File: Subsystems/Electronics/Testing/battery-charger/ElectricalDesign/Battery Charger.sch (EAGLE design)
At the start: 98 parts, among them J1 USB4515-GF-A_REVA, Q1 CSD16406Q3, Q2 CSD16406Q3, Q3 DMN2008LFU, Q4 DMN2008LFU, Q5 DMN2008LFU, Q6 BC817, Q7 BC817, U1 BQ24650, U2 BQ29700, U3 BQ29700, U4 BQ29700, U5 CP2102N-A02-GQFN28, U7 ESP32-S2-MINI-1

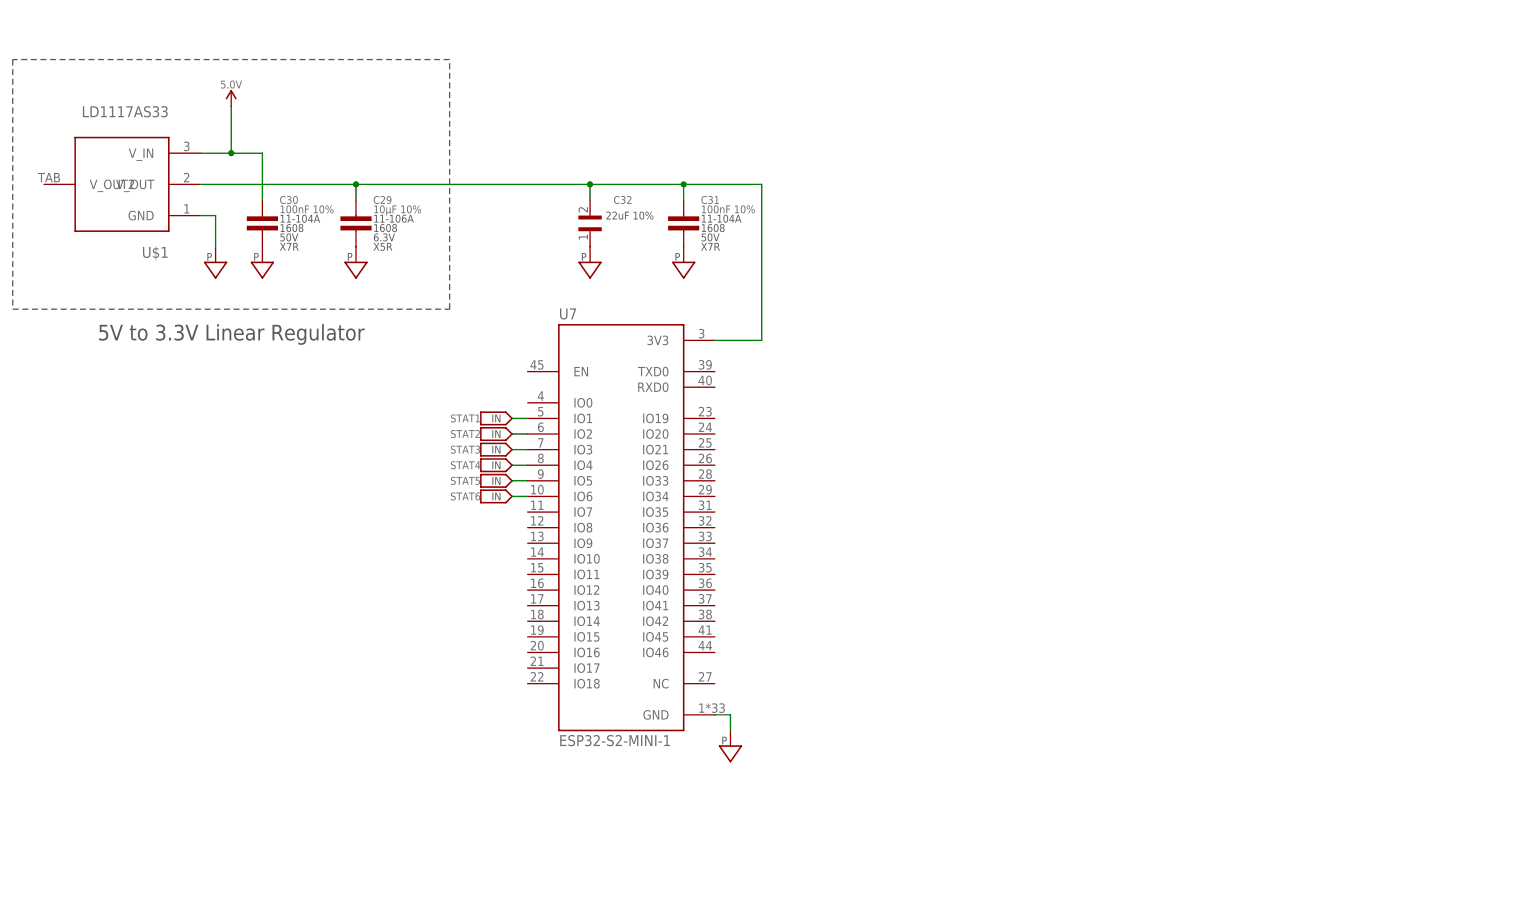
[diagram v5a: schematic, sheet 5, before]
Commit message: Finished Battery Charger V1
Will add programmable RGB LEDS at some point, and may update at a later date with an LED display, but otherwise this can be considered the base design for the over-engineered battery charger
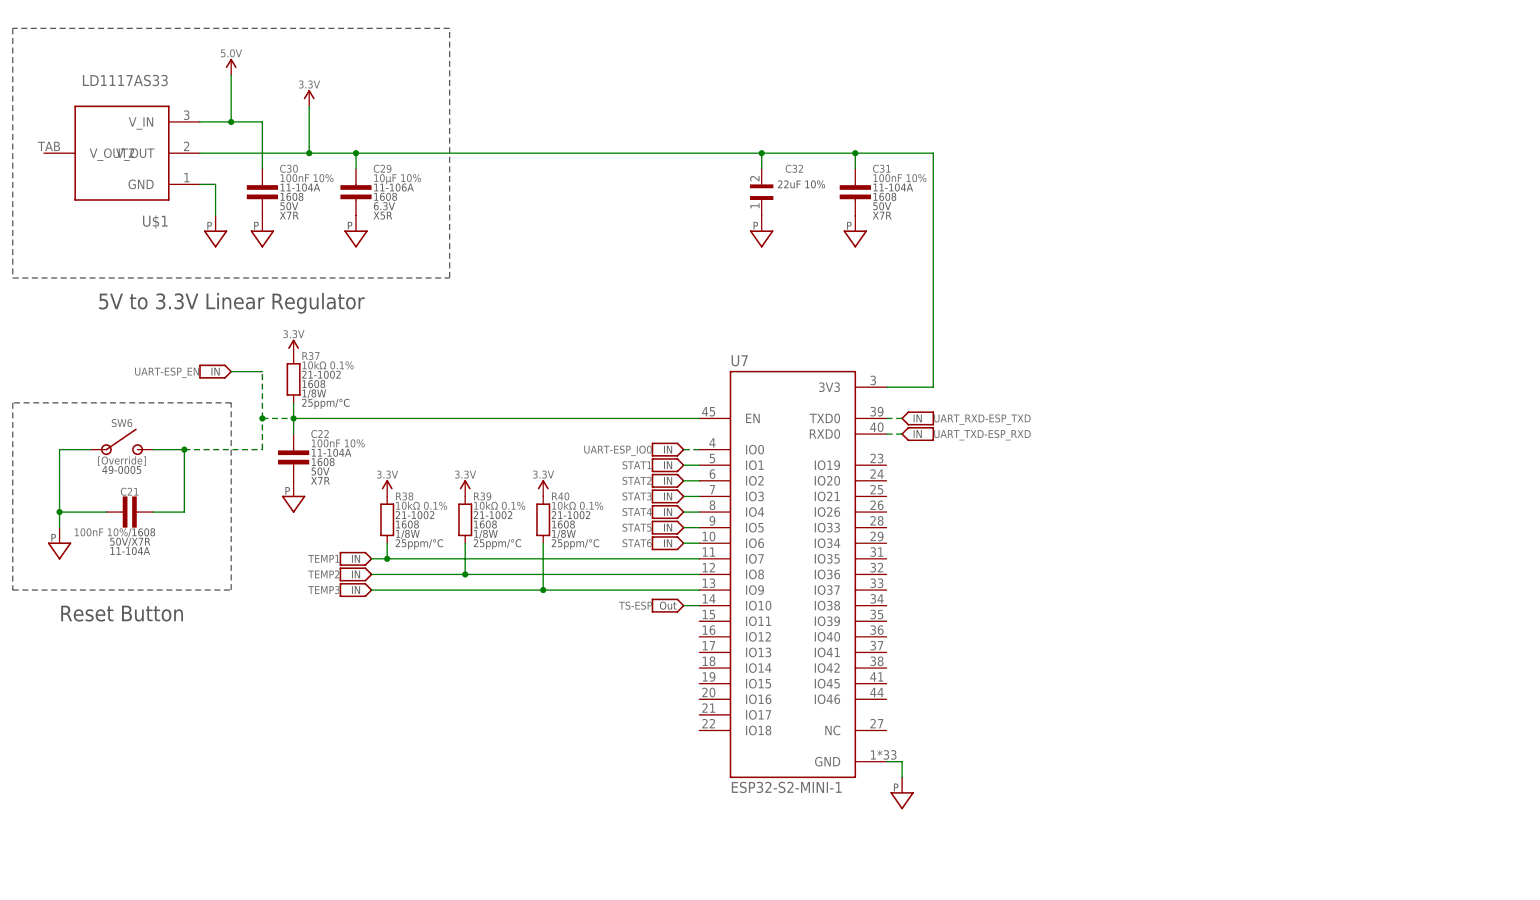
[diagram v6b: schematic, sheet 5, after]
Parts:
- removed J2: (no value), CougsInSpace-Connectors:USB-B-FEMALE
- added C21: 100nF 10%, CougsInSpace-Capacitors:CAP-H-100NF-1608
- added C22: 100nF 10%, CougsInSpace-Capacitors:CAP-V-100NF-1608
- added J3: 10103592-0001LF, 10103592-0001LF:10103592-0001LF
- added R37, R38, R39, R40: 10kΩ 0.1%, CougsInSpace-Resistors:RES-V-10K-1608
- added RT1, RT2, RT3: 10kΩ 5%, CougsInSpace-Resistors:THERMISTOR-V-10K-1608
- added SW6: [Override], CougsInSpace-Switches:SWITCH-SPST-NO-B3F-1050-THT-6060
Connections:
- removed net N$44: C29.1, C31.1, C32.2, U$1.V_OUT, U7.3V3
- new net 3.3V: C29.1, C31.1, C32.2, R37.2, R38.2, R39.2, R40.2, U$1.V_OUT, U7.3V3
- new net TEMP1: R38.1, RT1.2, U7.IO7
- new net TEMP2: R39.1, RT2.2, U7.IO8
- new net TEMP3: R40.1, RT3.2, U7.IO9
- new net TS-ESP: U1.TS, U7.IO10
- net N$25: now also J3.D+; no longer J2.DATA_P
- net N$31: now also J3.D-; no longer J2.DATA_N
- net N$42: now also J3.VDD; no longer J2.VCC
- net PGND: now also C21.1, C22.2, J3.GND, J3.SHIELD, RT1.1, RT2.1, RT3.1, SW6.COM; no longer J2.GND, J2.SHIELD
- net UART-ESP_EN: now also C21.2, C22.1, R37.1, SW6.NO, U7.EN
- net UART-ESP_IO0: now also U7.IO0
- net UART_RXD-ESP_TXD: now also U7.TXD0
- net UART_TXD-ESP_RXD: now also U7.RXD0
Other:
- note added: "CAD Note: Thermally Connected"
- note added: "Reset Button"
- note removed: "Change"
- moved on the sheet: BT3, C11, C29, C30, C31, C32, Q5, R14, R15, R16, R17, U$1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

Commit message: Added RGB LEDs
Final touches for V1 including CAD notes and addressable LEDs have been added
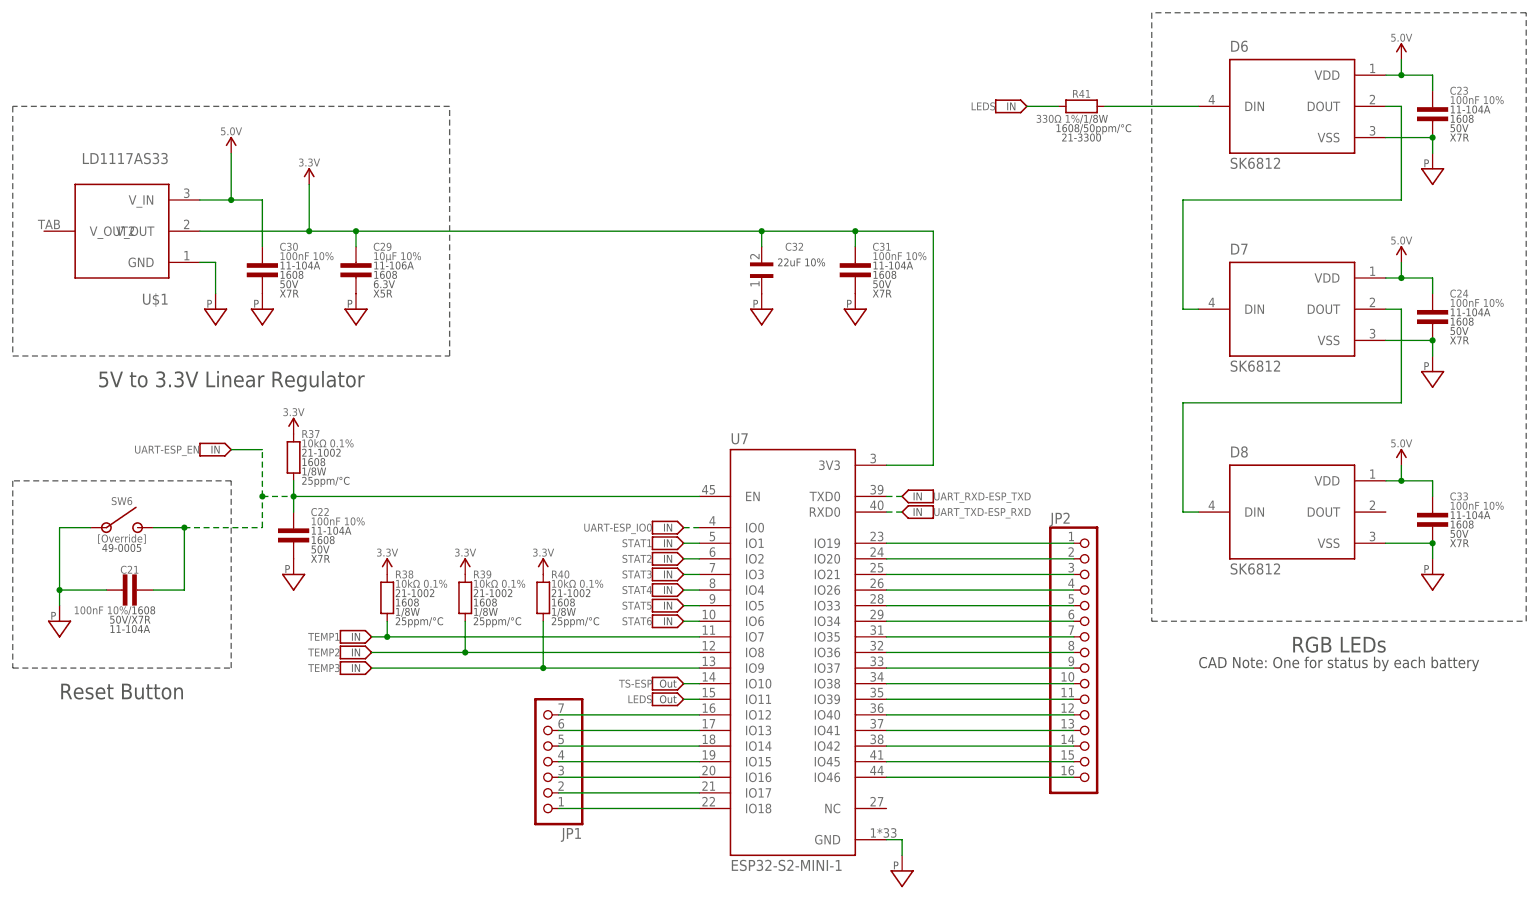
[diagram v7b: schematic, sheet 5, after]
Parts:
- added C23, C24, C33: 100nF 10%, CougsInSpace-Capacitors:CAP-V-100NF-1608
- added D6, D7, D8: SK6812, SK6812:SK6812
- added JP1: (no value), pinhead:PINHD-1X7
- added JP2: (no value), pinhead:PINHD-1X16
- added R41: 330Ω 1%, CougsInSpace-Resistors:RES-H-330R-1608
- DS1: value Red -> Yellow; device CougsInSpace-LEDs:LED-V-RED-1608 -> CougsInSpace-LEDs:LED-V-YLW-1608
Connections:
- new net LEDS: R41.1, U7.IO11
- new net N$44: JP2.1, U7.IO19
- new net N$52: JP2.2, U7.IO20
- new net N$53: JP2.3, U7.IO21
- new net N$54: JP2.4, U7.IO26
- new net N$55: JP2.5, U7.IO33
- new net N$56: JP2.6, U7.IO34
- new net N$57: JP2.7, U7.IO35
- new net N$58: JP2.8, U7.IO36
- new net N$59: JP2.9, U7.IO37
- new net N$60: JP2.10, U7.IO38
- new net N$61: JP2.11, U7.IO39
- new net N$62: JP2.12, U7.IO40
- new net N$63: JP2.13, U7.IO41
- new net N$64: JP2.14, U7.IO42
- new net N$65: JP2.15, U7.IO45
- new net N$66: JP2.16, U7.IO46
- new net N$67: D7.DOUT, D8.DIN
- new net N$68: JP1.7, U7.IO12
- new net N$69: JP1.6, U7.IO13
- new net N$70: JP1.5, U7.IO14
- new net N$71: JP1.4, U7.IO15
- new net N$72: JP1.3, U7.IO16
- new net N$73: JP1.2, U7.IO17
- new net N$74: JP1.1, U7.IO18
- new net N$76: D6.DOUT, D7.DIN
- new net N$77: D6.DIN, R41.2
- net 5.0V: now also C23.1, C24.1, C33.1, D6.VDD, D7.VDD, D8.VDD
- net PGND: now also C23.2, C24.2, C33.2, D6.VSS, D7.VSS, D8.VSS
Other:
- note added: "CAD Note: One for status by each battery"
- note added: "RGB LEDs"
- moved on the sheet: C21, C22, C29, C30, C31, C32, R37, R38, R39, R40, SW6, U$1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

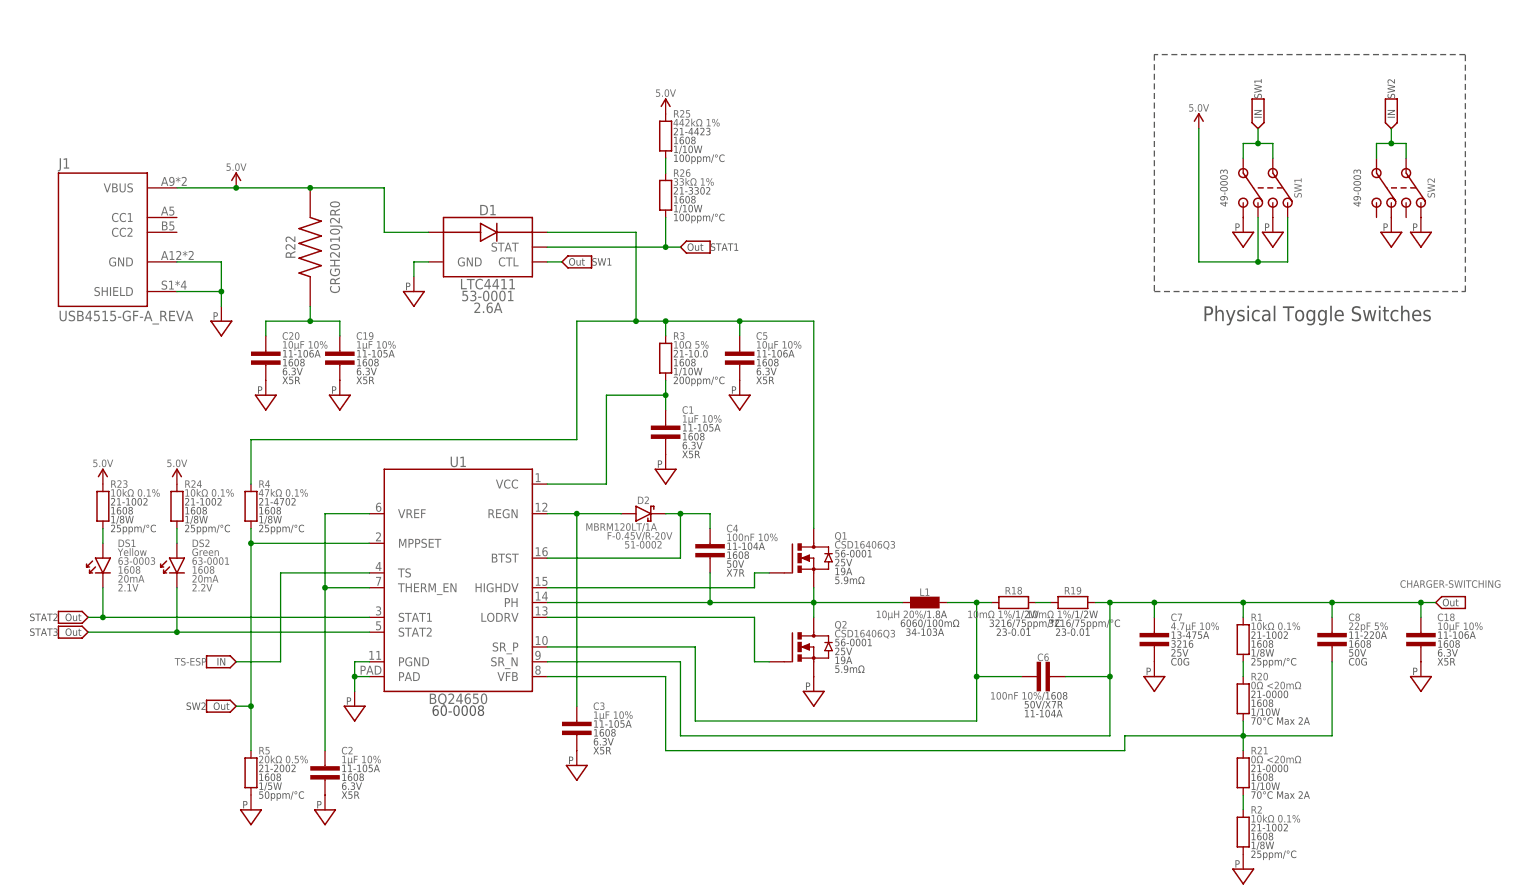
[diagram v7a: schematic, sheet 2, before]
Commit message: Tidied Up Schematic
Named all major nets, formatted in and out markings to match other CIS schematics, and adjusted LED colors to match convention.
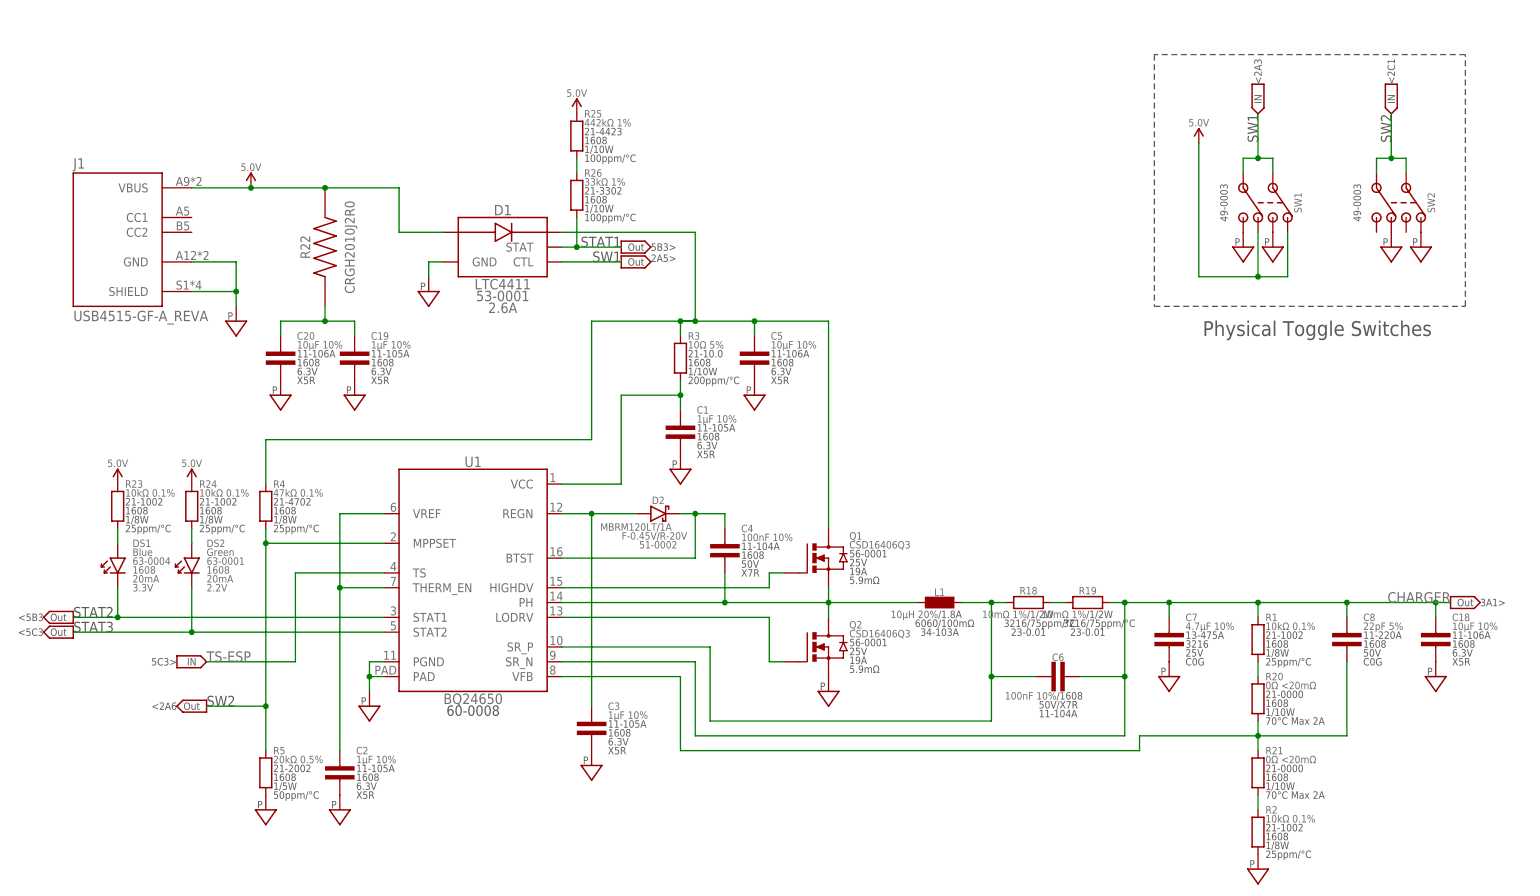
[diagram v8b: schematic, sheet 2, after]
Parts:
- DS1: value Yellow -> Blue; device CougsInSpace-LEDs:LED-V-YLW-1608 -> CougsInSpace-LEDs:LED-V-BLU-1608
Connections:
- net CHARGER-SWITCHING renamed CHARGER
- net N$1 renamed BQ24650_VREF
- net N$10 renamed BQ24650_HIGHDV
- net N$12 renamed BQ24650_LODRV
- net N$13 renamed BQ297001_V-
- net N$14 renamed BQ297002_V-
- net N$16 renamed BQ297001_COUT
- net N$17 renamed BQ297001_DOUT
- net N$18 renamed BQ297001_VSS
- net N$19 renamed BQ297002_COUT
- net N$2 renamed D1_OUT
- net N$20 renamed BQ297001_BAT
- net N$21 renamed CP2102N_VDD
- net N$22 renamed BQ297002_DOUT
- net N$23 renamed BQ297002_VSS
- net N$24 renamed BQ297002_BAT
- net N$25 renamed D+
- net N$26 renamed BQ297003_V-
- net N$27 renamed BQ297003_COUT
- net N$28 renamed BQ297003_DOUT
- net N$29 renamed BQ297003_VSS
- net N$3 renamed BQ24650_REGN
- net N$30 renamed BQ297003_BAT
- net N$31 renamed D-
- net N$39 renamed D3_OUT
- net N$4 renamed BQ24650_PH
- net N$40 renamed D4_OUT
- net N$41 renamed D5_OUT
- net N$42 renamed USB_VDD
- net N$43 renamed CP2102N_RXT
- net N$44 renamed ESP32_IO19
- net N$45 renamed CP2102N_TXT
- net N$46 renamed CP2102N_RTS
- net N$47 renamed CP2102N_DTR
- net N$5 renamed BQ24650_BTST
- net N$52 renamed ESP32_IO20
- net N$53 renamed ESP32_IO21
- net N$54 renamed ESP32_IO26
- net N$55 renamed ESP32_IO33
- net N$56 renamed ESP32_IO34
- net N$57 renamed ESP32_IO35
- net N$58 renamed ESP32_IO36
- net N$59 renamed ESP32_IO37
- net N$6 renamed BQ24650_VCC
- net N$60 renamed ESP32_IO38
- net N$61 renamed ESP32_IO39
- net N$62 renamed ESP32_IO40
- net N$63 renamed ESP32_IO41
- net N$64 renamed ESP32_IO42
- net N$65 renamed ESP32_IO45
- net N$66 renamed ESP32_IO46
- net N$67 renamed LED3_DIN
- net N$68 renamed ESP32_IO12
- net N$69 renamed ESP32_IO13
- net N$7 renamed BQ24650_SR_P
- net N$70 renamed ESP32_IO14
- net N$71 renamed ESP32_IO15
- net N$72 renamed ESP32_IO16
- net N$73 renamed ESP32_IO17
- net N$74 renamed ESP32_IO18
- net N$76 renamed LED2_DIN
- net N$77 renamed LED1_DIN
- net N$9 renamed BQ24650_VFB
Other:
- note added: "2A3>"
- note added: "2A5>"
- note added: "2C1>"
- note added: "2C6>"
- note added: "3A1>"
- note added: "3A2>"
- note added: "3A6>"
- note added: "3B2>"
- note added: "3B6>"
- note added: "3C2>"
- note added: "3C4>"
- note added: "3C5>"
- note added: "3C6>"
- note added: "4B6>"
- note added: "4C6>"
- note added: "5B1>"
- note added: "5B3>"
- note added: "5B5>"
- note added: "5C3>"
- note added: "<2A3"
- note added: "<2A6"
- note added: "<2C1"
- note added: "<3A2"
- note added: "<3B2"
- note added: "<3C2"
- note added: "<4B6"
- note added: "<5A4"
- note added: "<5B3"
- note added: "<5B5"
- note added: "<5C2"
- note added: "<5C3"
- moved on the sheet: BT2, C1, C10, C15, C16, C17, C18, C19, C2, C20, C3, C4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
